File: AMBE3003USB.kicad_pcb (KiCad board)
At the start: 2 copper layers, 72.6 x 71.6 mm, 97 parts, among them J1 McBSP, J2 ACONF, J3 CODEC, J4 USB_OTG, P1 CONFIG, U1 AMBE3003, U2 LD1117S33TR, U3 TPS3805, U4 FT232RL, U5 TPS78319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

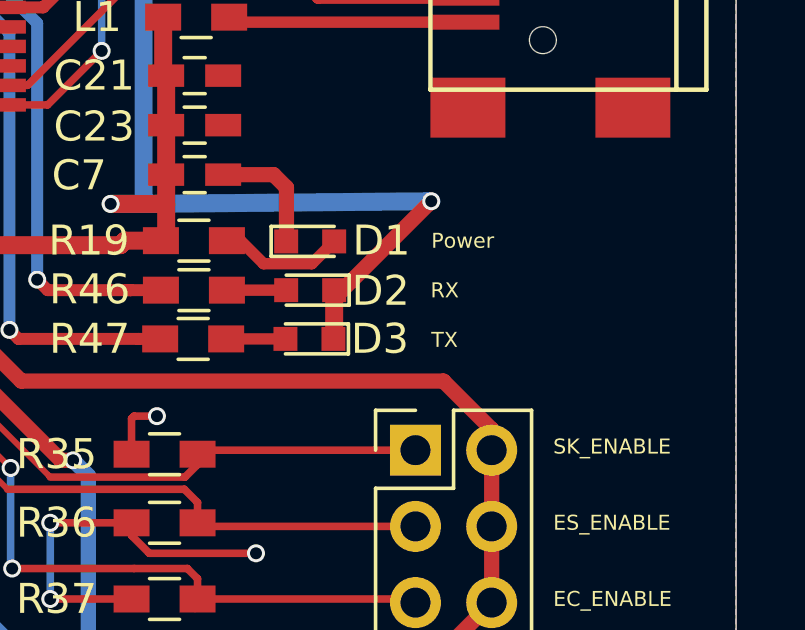
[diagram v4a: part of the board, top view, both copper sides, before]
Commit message: Better reverse RX/TX LEDs
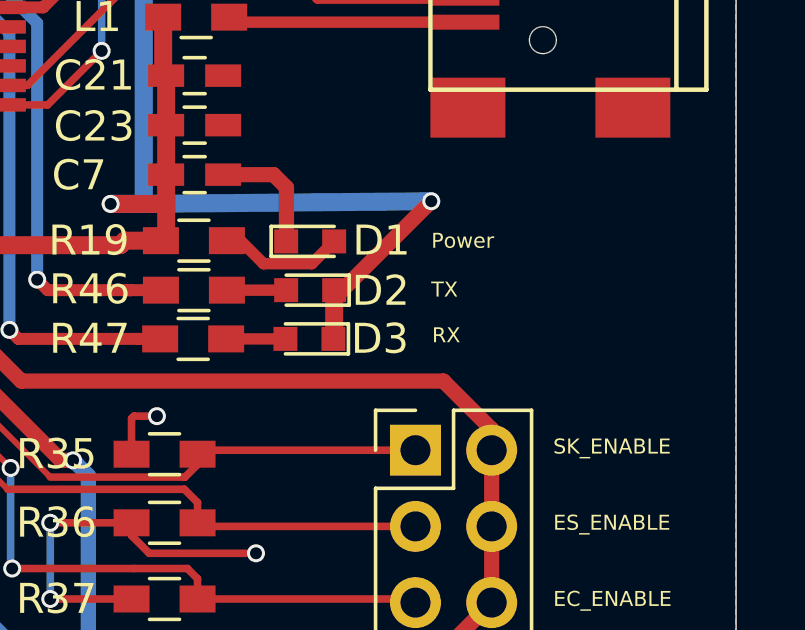
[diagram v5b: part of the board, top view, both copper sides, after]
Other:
- net class 0.2mm: clearance 0.1 -> 0.2
- net class 0.5mm: clearance 0.1 -> 0.2
- net class Default: clearance 0.1 -> 0.2
- rule trace_clearance: 0.1 -> 0.2
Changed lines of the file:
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@@
     (user_trace_width 0.508)
     (user_trace_width 0.8128)
-    (trace_clearance 0.1)
+    (trace_clearance 0.2)
     (zone_clearance 0.508)
     (zone_45_only no)
@@
   (net 132 /ES_ENABLE)
   (net_class Default "Dies ist die voreingestellte Netzklasse."
-    (clearance 0.1)
+    (clearance 0.2)
     (trace_width 0.25)
     (via_dia 0.6)
@@
   )
   (net_class 0.2mm ""
-    (clearance 0.1)
+    (clearance 0.2)
     (trace_width 0.2)
     (via_dia 0.6)
@@
   )
   (net_class 0.5mm ""
-    (clearance 0.1)
+    (clearance 0.2)
     (trace_width 0.5)
     (via_dia 0.6)
@@
     (pad 1 thru_hole circle (at 0 0) (size 4.064 4.064) (drill 3.048) (layers *.Cu *.Mask F.SilkS))
   )
-  (gr_text RX (at 110.2106 73.533) (layer F.SilkS)
+  (gr_text RX (at 110.2614 75.0316) (layer F.SilkS)
     (effects (font (size 0.5 0.5) (thickness 0.1)) (justify left))
   )
-  (gr_text TX (at 110.236 75.184) (layer F.SilkS)
+  (gr_text TX (at 110.236 73.5076) (layer F.SilkS)
     (effects (font (size 0.5 0.5) (thickness 0.1)) (justify left))
   )

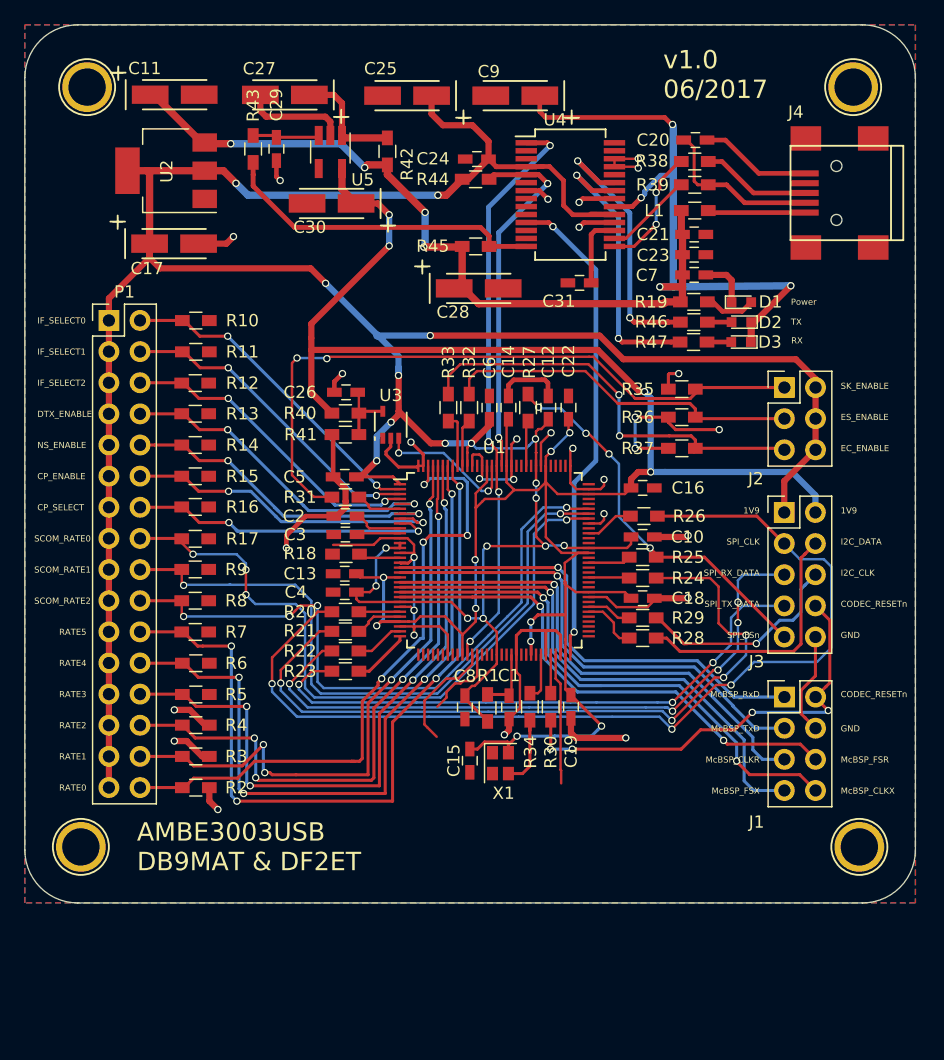
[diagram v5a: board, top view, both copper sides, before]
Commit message: Re-route the PCB layout
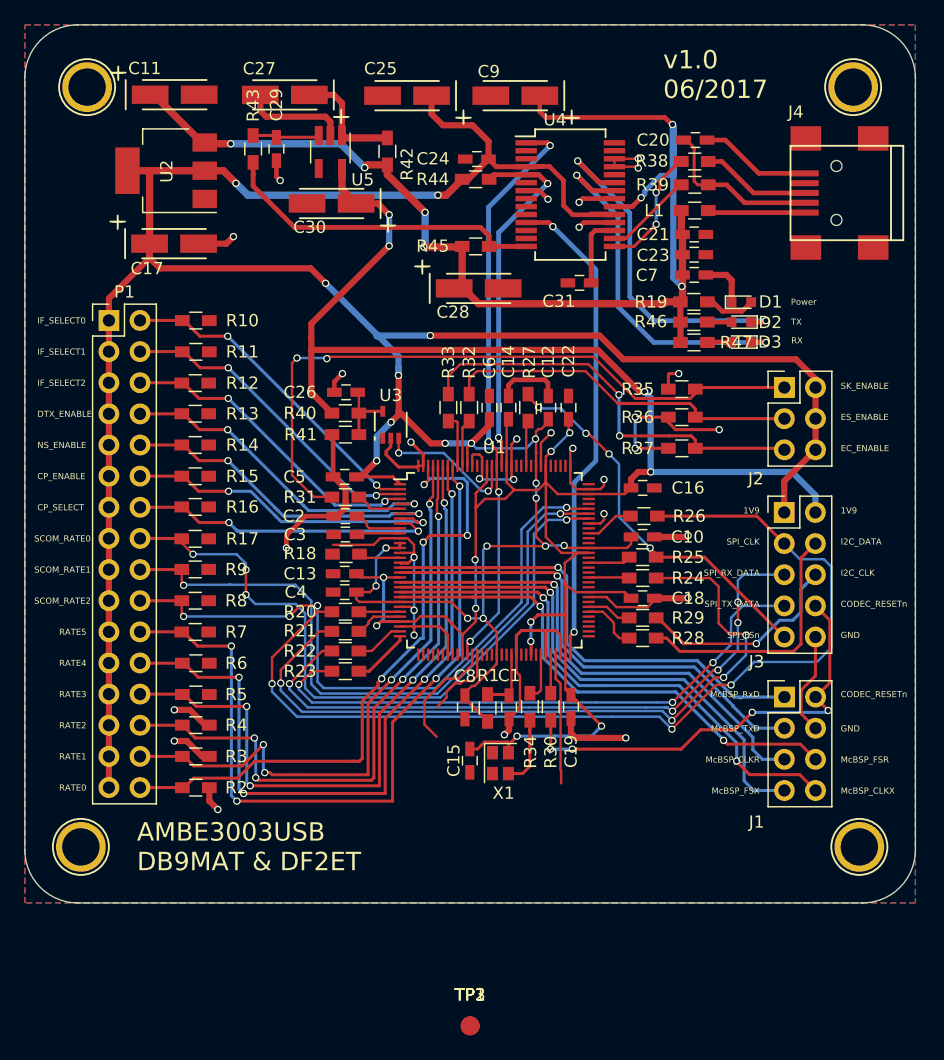
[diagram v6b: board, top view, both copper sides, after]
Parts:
- added TP1: STANDBY, Measurement_Points:Measurement_Point_Round-SMD-Pad_Small, F.Cu at (84.1, 130.9)
- added TP2: IDLE, Measurement_Points:Measurement_Point_Round-SMD-Pad_Small, F.Cu at (84.1, 130.9)
- added TP3: RUN, Measurement_Points:Measurement_Point_Round-SMD-Pad_Small, F.Cu at (84.1, 130.9)
- turned R47 to 0 degrees
- turned R46 to 0 degrees
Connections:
- D2 pad 1: +5V -> Net-(D2-Pad1)
- D3 pad 1: +5V -> Net-(D3-Pad1)
- J4 pad 6: GND -> Net-(J4-Pad6)
- R46 pad 1: Net-(D2-Pad2) -> +5V
- R46 pad 2: Net-(R46-Pad2) -> Net-(D2-Pad2)
- R47 pad 1: Net-(D3-Pad2) -> +5V
- R47 pad 2: Net-(R47-Pad2) -> Net-(D3-Pad2)
- U4 pad 22: Net-(R47-Pad2) -> Net-(D3-Pad1)
- U4 pad 23: Net-(R46-Pad2) -> Net-(D2-Pad1)
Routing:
- net Net-(D3-Pad1): track 0.00 -> 30.3 mm, vias 0 -> 2
- net Net-(D2-Pad1): track 0.00 -> 29.7 mm, vias 0 -> 2
- net Net-(R47-Pad2): track 23.5 -> 0.00 mm, vias 2 -> 0
- net Net-(R46-Pad2): track 22.7 -> 0.00 mm, vias 2 -> 0
- net +5V: track 114.9 -> 100.0 mm, vias 8 -> 7

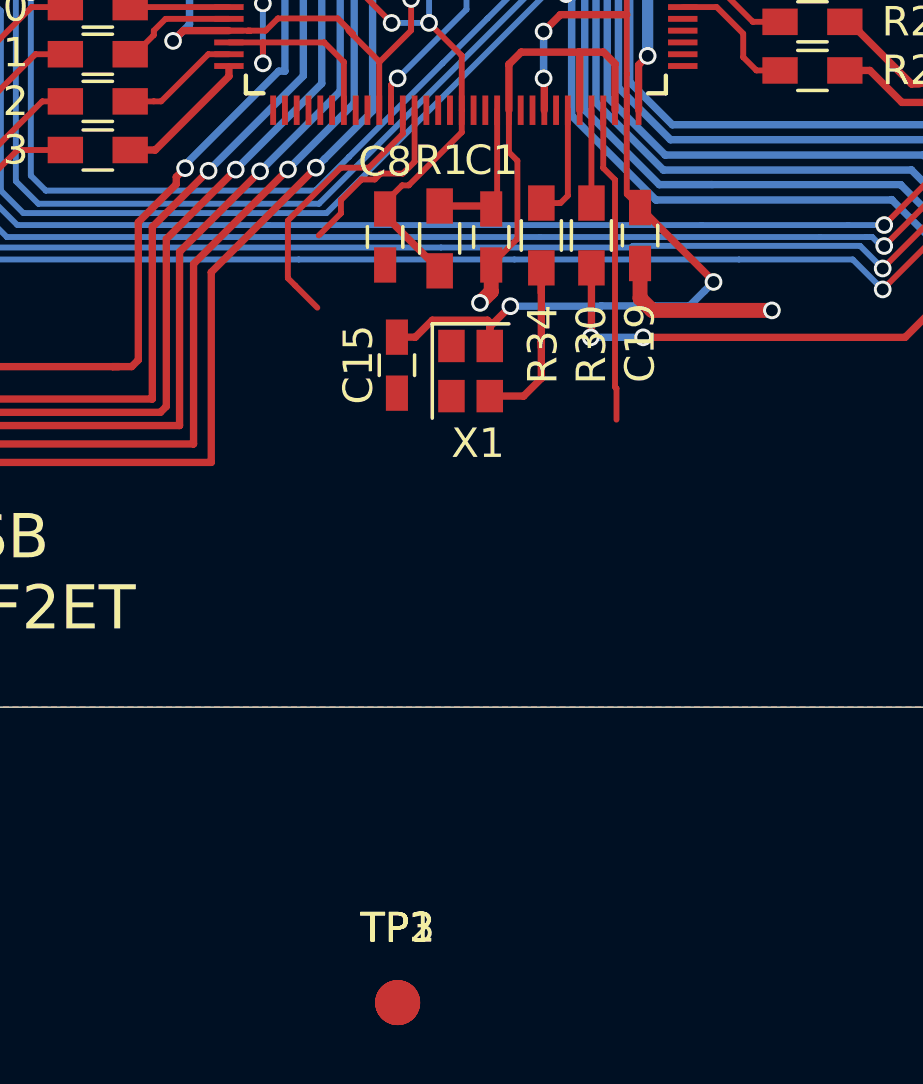
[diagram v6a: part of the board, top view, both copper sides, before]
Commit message: Add Testpad for GND
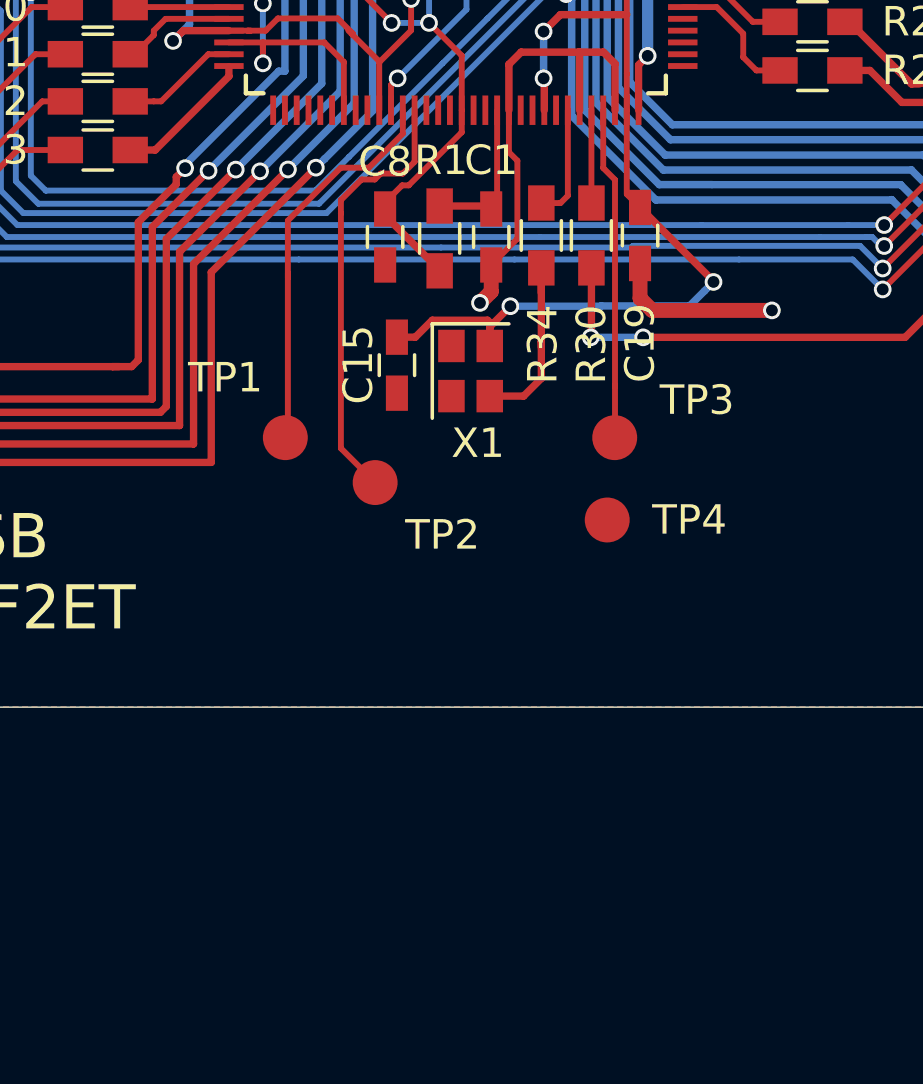
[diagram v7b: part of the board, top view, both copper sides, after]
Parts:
- added TP4: GND, Measurement_Points:Measurement_Point_Round-SMD-Pad_Small, F.Cu at (91.2, 114.6)
- moved TP3 20.5 mm to (91.4, 111.8)
- moved TP1 19.5 mm to (80.3, 111.8)
- moved TP2 17.7 mm to (83.3, 113.3)
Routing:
- net /_IDLE: track 6.30 -> 14.9 mm
- net /_STANDBY: track 9.29 -> 13.6 mm
- net /_RUN: track 10.7 -> 11.3 mm
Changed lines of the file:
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@@
 (kicad_pcb (version 4) (host pcbnew 4.0.2+dfsg1-stable)
   (general
-    (links 270)
-    (no_connects 6)
+    (links 271)
+    (no_connects 4)
     (area 47.726499 49.250499 120.421501 120.929501)
     (thickness 1.6)
     (drawings 50)
-    (tracks 1336)
+    (tracks 1340)
     (zones 0)
-    (modules 100)
+    (modules 101)
     (nets 134)
   )
@@
   )
   (setup
-    (last_trace_width 0.508)
+    (last_trace_width 0.25)
     (user_trace_width 0.2)
     (user_trace_width 0.254)
@@
   )
   (module Measurement_Points:Measurement_Point_Round-SMD-Pad_Small (layer F.Cu)
-    (at 84.074 130.929501)
+    (at 80.264 111.76)
     (descr "Mesurement Point, Round, SMD Pad, DM 1.5mm,")
     (tags "Mesurement Point, Round, SMD Pad, DM 1.5mm,")
-    (fp_text reference TP1 (at 0 -2.54) (layer F.SilkS)
+    (fp_text reference TP1 (at -2.032 -2.032) (layer F.SilkS)
       (effects (font (size 1 1) (thickness 0.15)))
     )
-    (fp_text value STANDBY (at 1.27 2.54) (layer F.Fab)
+    (fp_text value STANDBY (at -2.286 2.286) (layer F.Fab)
       (effects (font (size 1 1) (thickness 0.15)))
     )
@@
   )
   (module Measurement_Points:Measurement_Point_Round-SMD-Pad_Small (layer F.Cu)
-    (at 84.074 130.929501)
+    (at 83.312 113.284)
     (descr "Mesurement Point, Round, SMD Pad, DM 1.5mm,")
     (tags "Mesurement Point, Round, SMD Pad, DM 1.5mm,")
-    (fp_text reference TP2 (at 0 -2.54) (layer F.SilkS)
+    (fp_text reference TP2 (at 2.286 1.778) (layer F.SilkS)
       (effects (font (size 1 1) (thickness 0.15)))
     )
-    (fp_text value IDLE (at 1.27 2.54) (layer F.Fab)
+    (fp_text value IDLE (at -1.27 2.032) (layer F.Fab)
       (effects (font (size 1 1) (thickness 0.15)))
     )
@@
   )
   (module Measurement_Points:Measurement_Point_Round-SMD-Pad_Small (layer F.Cu)
-    (at 84.074 130.929501)
+    (at 91.44 111.76)
     (descr "Mesurement Point, Round, SMD Pad, DM 1.5mm,")
     (tags "Mesurement Point, Round, SMD Pad, DM 1.5mm,")
-    (fp_text reference TP3 (at 0 -2.54) (layer F.SilkS)
+    (fp_text reference TP3 (at 2.794 -1.27) (layer F.SilkS)
       (effects (font (size 1 1) (thickness 0.15)))
     )
-    (fp_text value RUN (at 1.27 2.54) (layer F.Fab)
+    (fp_text value RUN (at 3.81 0.254) (layer F.Fab)
       (effects (font (size 1 1) (thickness 0.15)))
     )
@@
       (net 123 /_RUN))
   )
+  (module Measurement_Points:Measurement_Point_Round-SMD-Pad_Small (layer F.Cu)
+    (at 91.186 114.554)
+    (descr "Mesurement Point, Round, SMD Pad, DM 1.5mm,")
+    (tags "Mesurement Point, Round, SMD Pad, DM 1.5mm,")
+    (fp_text reference TP4 (at 2.794 0) (layer F.SilkS)
+      (effects (font (size 1 1) (thickness 0.15)))
+    )
+    (fp_text value GND (at 0.762 2.032) (layer F.Fab)
+      (effects (font (size 1 1) (thickness 0.15)))
+    )
+    (pad 1 smd circle (at 0 0) (size 1.524 1.524) (layers F.Cu F.Paste F.Mask)
+      (net 1 GND))
+  )
   (gr_text RX (at 110.2614 75.0316) (layer F.SilkS)
     (effects (font (size 0.5 0.5) (thickness 0.1)) (justify left))
@@
   (segment (start 100.65 57.675) (end 100.65 57.47) (width 0.508) (layer B.Cu) (net 3))
   (segment (start 99.613998 61.55) (end 100.65 61.55) (width 0.4) (layer B.Cu) (net 3))
+  (segment (start 87.124999 107.774999) (end 85.250001 107.774999) (width 0.25) (layer F.Cu) (net 4))
+  (segment (start 87.2 107.85) (end 87.124999 107.774999) (width 0.25) (layer F.Cu) (net 4))
+  (segment (start 85.250001 107.774999) (end 84.675 108.35) (width 0.25) (layer F.Cu) (net 4))
+  (segment (start 84.675 108.35) (end 84.05 108.35) (width 0.25) (layer F.Cu) (net 4))
+  (segment (start 87.2 108.65) (end 87.2 107.85) (width 0.25) (layer F.Cu) (net 4))
   (segment (start 87.6681 87.2109) (end 86.9315 87.9475) (width 0.2) (layer F.Cu) (net 4))
   (segment (start 84.582 88.646) (end 85.09 88.138) (width 0.2) (layer F.Cu) (net 4))
@@
   (segment (start 77.0128 94.35) (end 75.1 94.35) (width 0.2) (layer F.Cu) (net 4))
   (segment (start 75.1 94.35) (end 74.8 94.05) (width 0.2) (layer F.Cu) (net 4))
-  (segment (start 87.2 108.65) (end 87.2 107.85) (width 0.25) (layer F.Cu) (net 4))
-  (segment (start 84.675 108.35) (end 84.05 108.35) (width 0.25) (layer F.Cu) (net 4))
-  (segment (start 85.250001 107.774999) (end 84.675 108.35) (width 0.25) (layer F.Cu) (net 4))
-  (segment (start 87.124999 107.774999) (end 85.250001 107.774999) (width 0.25) (layer F.Cu) (net 4))
-  (segment (start 87.2 107.85) (end 87.124999 107.774999) (width 0.25) (layer F.Cu) (net 4))
   (segment (start 84.05 108.125) (end 84.05 108.35) (width 0.25) (layer F.Cu) (net 4))
   (segment (start 75 80.95) (end 75 79.35) (width 0.2) (layer F.Cu) (net 5))
@@
   (segment (start 83.05 81.7) (end 82.95 81.6) (width 0.2) (layer F.Cu) (net 120))
   (segment (start 82.95 81.6) (end 82.3 81.6) (width 0.2) (layer F.Cu) (net 120))
-  (segment (start 80.349999 106.349999) (end 80.600001 106.600001) (width 0.2) (layer F.Cu) (net 121))
-  (segment (start 80.349999 104.395999) (end 80.349999 106.349999) (width 0.2) (layer F.Cu) (net 121))
-  (segment (start 80.600001 106.600001) (end 81.35 107.35) (width 0.2) (layer F.Cu) (net 121))
+  (segment (start 80.349999 106.172) (end 80.349999 111.337999) (width 0.2) (layer F.Cu) (net 121))
+  (segment (start 80.349999 111.337999) (end 80.772 111.76) (width 0.2) (layer F.Cu) (net 121))
+  (segment (start 80.349999 104.395999) (end 80.349999 106.172) (width 0.2) (layer F.Cu) (net 121))
+  (segment (start 80.349999 106.172) (end 80.349999 106.349999) (width 0.2) (layer F.Cu) (net 121))
   (segment (start 82.146008 102.59999) (end 80.349999 104.395999) (width 0.2) (layer F.Cu) (net 121))
   (segment (start 83.10001 102.59999) (end 82.146008 102.59999) (width 0.2) (layer F.Cu) (net 121))
   (segment (start 84.25 101.45) (end 83.10001 102.59999) (width 0.2) (layer F.Cu) (net 121))
   (segment (start 84.25 100.65) (end 84.25 101.45) (width 0.2) (layer F.Cu) (net 121))
-  (segment (start 81.4 104.9) (end 82.149999 104.150001) (width 0.2) (layer F.Cu) (net 122))
-  (segment (start 82.149999 104.150001) (end 82.149999 103.700001) (width 0.2) (layer F.Cu) (net 122))
+  (segment (start 82.149999 104.14) (end 82.149999 112.121999) (width 0.2) (layer F.Cu) (net 122))
+  (segment (start 82.149999 112.121999) (end 83.312 113.284) (width 0.2) (layer F.Cu) (net 122))
+  (segment (start 82.149999 104.150001) (end 82.149999 104.14) (width 0.2) (layer F.Cu) (net 122))
+  (segment (start 82.149999 104.14) (end 82.149999 103.700001) (width 0.2) (layer F.Cu) (net 122))
   (segment (start 82.149999 103.700001) (end 82.85 103) (width 0.2) (layer F.Cu) (net 122))
   (segment (start 82.85 103) (end 83.3 103) (width 0.2) (layer F.Cu) (net 122))
@@
   (segment (start 84.65 102.4) (end 84.25001 102.79999) (width 0.2) (layer F.Cu) (net 122))
   (segment (start 84.65 100.65) (end 84.65 102.4) (width 0.2) (layer F.Cu) (net 122))
-  (segment (start 91.5 110.08934) (end 91.5 111.15) (width 0.2) (layer F.Cu) (net 123))
-  (segment (start 91.44999 103.009988) (end 91.44999 110.03933) (width 0.2) (layer F.Cu) (net 123))
-  (segment (start 91.44999 110.03933) (end 91.5 110.08934) (width 0.2) (layer F.Cu) (net 123))
+  (segment (start 91.44999 109.982) (end 91.44999 111.75001) (width 0.2) (layer F.Cu) (net 123))
+  (segment (start 91.44999 111.75001) (end 91.44 111.76) (width 0.2) (layer F.Cu) (net 123))
+  (segment (start 91.44999 103.009988) (end 91.44999 109.982) (width 0.2) (layer F.Cu) (net 123))
+  (segment (start 91.44999 109.982) (end 91.44999 110.03933) (width 0.2) (layer F.Cu) (net 123))
   (segment (start 91.05 100.65) (end 91.05 102.609998) (width 0.2) (layer F.Cu) (net 123))
   (segment (start 91.05 102.609998) (end 91.44999 103.009988) (width 0.2) (layer F.Cu) (net 123))
